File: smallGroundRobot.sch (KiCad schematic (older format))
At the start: 0 parts

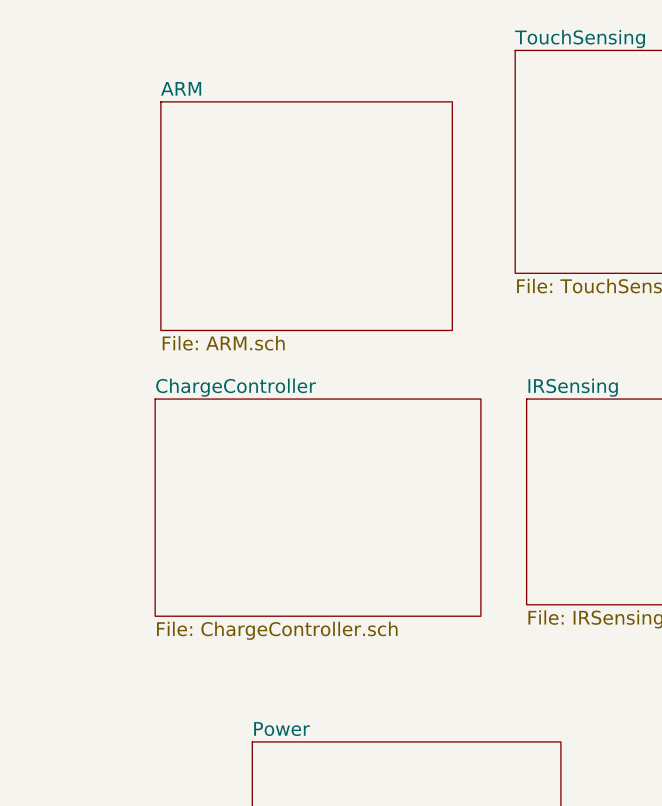
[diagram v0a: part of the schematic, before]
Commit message: Added power, touch, and motor controller
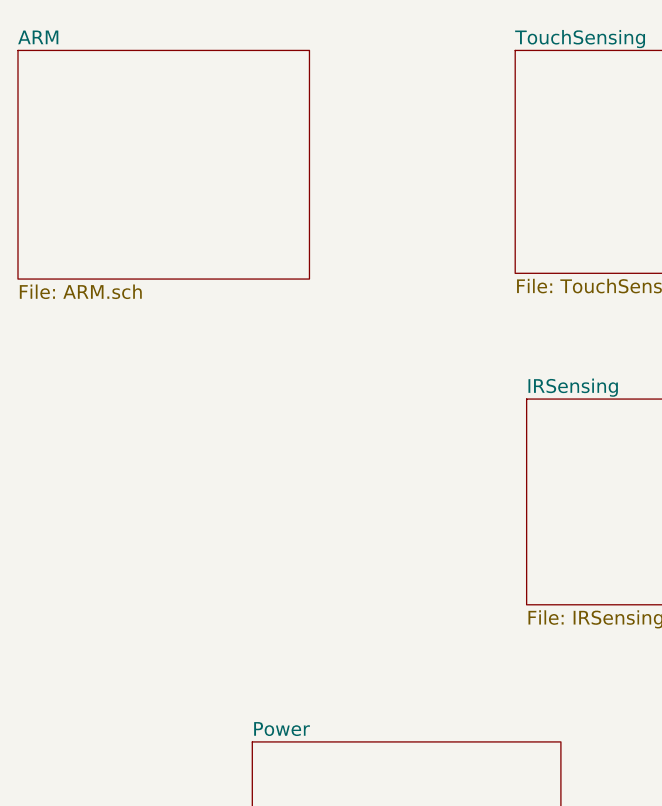
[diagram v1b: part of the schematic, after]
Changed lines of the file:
@@
 $Descr A4 11693 8268
 encoding utf-8
-Sheet 1 8
+Sheet 1 7
 Title ""
 Date ""
@@
 $EndSheet
 $Sheet
-S 4450 2475 1275 1000
+S 3825 2250 1275 1000
 U 5A7E3CFD
 F0 "ARM" 60
@@
 $EndSheet
 $Sheet
-S 4425 3775 1425 950
-U 5A7E3D38
-F0 "ChargeController" 60
-F1 "ChargeController.sch" 60
-$EndSheet
-$Sheet

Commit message: Finished Schematic
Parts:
- added D? (x3): LED, symbol LED
- added J? (x4): Conn_01x03, symbol Conn_01x03
- added J?: USB_OTG, symbol USB_OTG
- added Q? (x2): Q_NPN_BEC, symbol Q_NPN_BEC
- added R? (x2): 2, symbol R
- added R?: 39, symbol R
- added R? (x2): 22, symbol R
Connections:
- new net: J?.2 (Pin_2), Q?.1 (B) (x2)
- new net: Q?.3 (C), R?.2 (x2)
- new net: D?.1 (K), R?.1 (x2)
- new net: J?.2 (D-), R?.2
- new net: J?.3 (D+), R?.2
- new net: D?.1 (K), R?.2
- new net +3V3: J?.1 (Pin_1), J?.1 (Pin_1)
- new net 3V_L1: D?.2 (A), D?.2 (A), J?.3 (Pin_3), J?.3 (Pin_3)
- new net ARM/PB12: D?.2 (A)
- new net D+: R?.1
- new net D-: R?.1
- new net GND: J?.3 (Pin_3), J?.3 (Pin_3), J?.4 (ID), J?.5 (GND), J?.6 (Shield), R?.1
- new net GND_L1: J?.1 (Pin_1), J?.1 (Pin_1), Q?.2 (E), Q?.2 (E)
- new net L1: J?.2 (Pin_2)
- new net L2: J?.2 (Pin_2)
- new net USB5V: J?.1 (VBUS)
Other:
- note added: "Headlights"

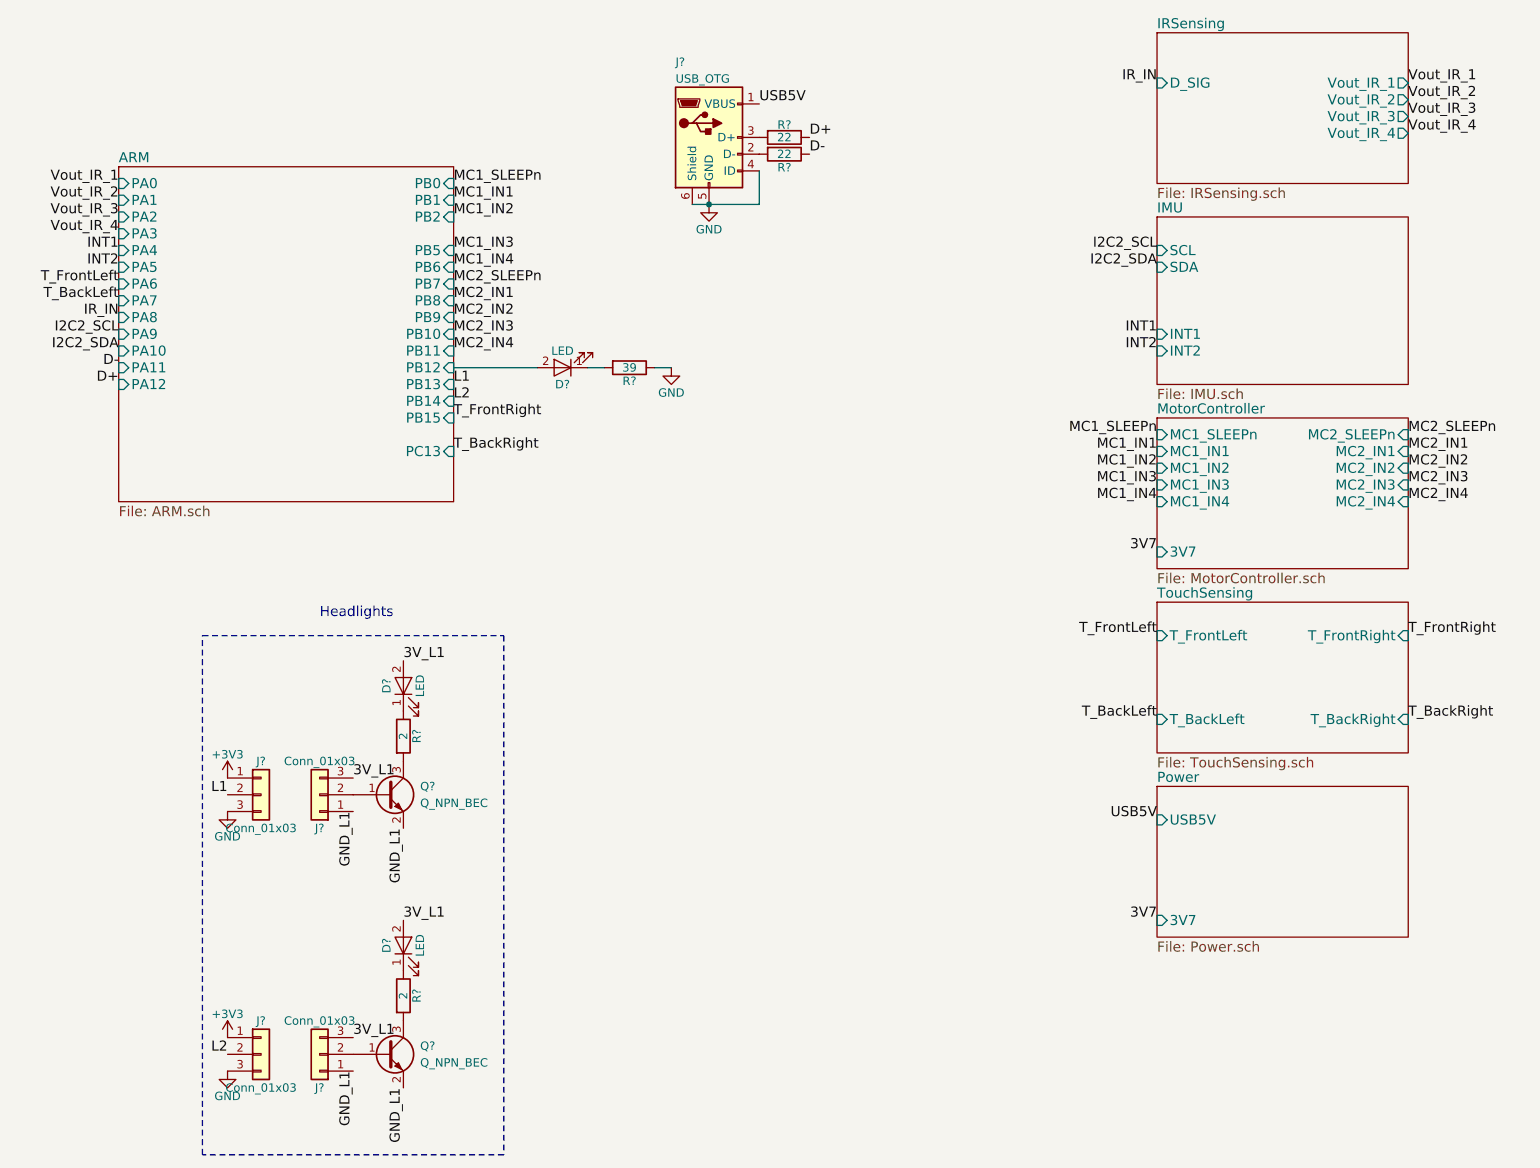
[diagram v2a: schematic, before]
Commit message: Started associating footprints
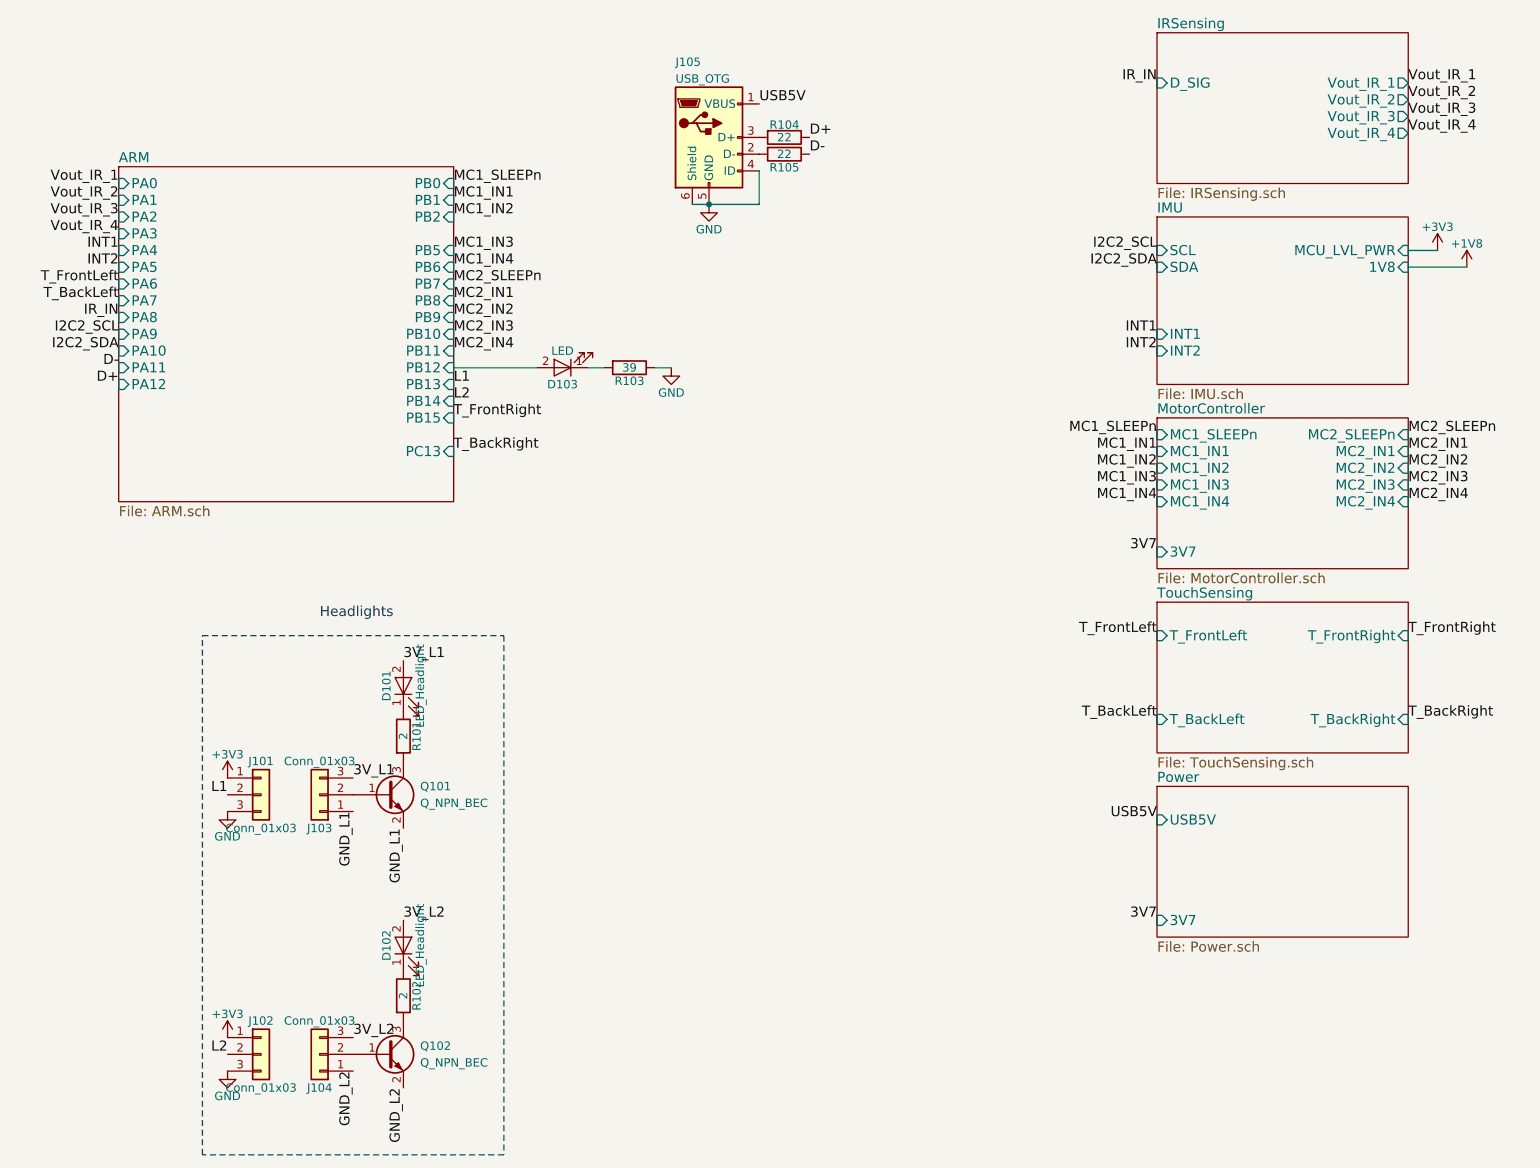
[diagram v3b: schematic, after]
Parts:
- D101, D102: renamed from D?; value LED -> LED_Headlight; footprint (none) -> LEDs:LED_1206
- D103: renamed from D?; footprint (none) -> LEDs:LED_0805
- J101, J102, J103, J104: renamed from J?; footprint (none) -> Pin_Headers:Pin_Header_Angled_1x03_Pitch1.27mm
- J105: renamed from J?; footprint (none) -> Connectors:USB_Micro-B
- gave numbers to parts that had none: 7
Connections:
- net 3V_L1: no longer D102.2 (A), J104.3 (Pin_3)
- net GND_L1: no longer J104.1 (Pin_1), Q102.2 (E)
- new net 3V_L2: D102.2 (A), J104.3 (Pin_3)
- new net GND_L2: J104.1 (Pin_1), Q102.2 (E)
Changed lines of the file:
@@
 F4 "INT1" I L 8000 2500 60
 F5 "INT2" I L 8000 2600 60
+F6 "MCU_LVL_PWR" I R 9500 2000 60
+F7 "1V8" I R 9500 2100 60
 $EndSheet
 $Sheet
@@
 MC2_IN4
 $Comp
-L LED D?
+L LED D103
 U 1 1 5AC53F8E
 P 4450 2700
-F 0 "D?" H 4450 2800 50  0000 C CNN
+F 0 "D103" H 4450 2800 50  0000 C CNN
 F 1 "LED" H 4450 2600 50  0000 C CNN
-F 2 "" H 4450 2700 50  0001 C CNN
+F 2 "LEDs:LED_0805" H 4450 2700 50  0001 C CNN
 F 3 "" H 4450 2700 50  0001 C CNN
 	1    4450 2700
@@
 $EndComp
 $Comp
-L R R?
+L R R103
 U 1 1 5AC54125
 P 4850 2700
-F 0 "R?" V 4930 2700 50  0000 C CNN
+F 0 "R103" V 4930 2700 50  0000 C CNN
 F 1 "39" V 4850 2700 50  0000 C CNN
 F 2 "" V 4780 2700 50  0001 C CNN
@@
 $EndComp
 $Comp
-L GND #PWR?
+L GND #PWR01
 U 1 1 5AC56677
 P 5100 2700
-F 0 "#PWR?" H 5100 2450 50  0001 C CNN
+F 0 "#PWR01" H 5100 2450 50  0001 C CNN
 F 1 "GND" H 5100 2550 50  0000 C CNN
 F 2 "" H 5100 2700 50  0001 C CNN
@@
 	4300 2700 3800 2700
 $Comp
-L Q_NPN_BEC Q?
+L Q_NPN_BEC Q101
 U 1 1 5AC13475
 P 3400 5250
-F 0 "Q?" H 3600 5300 50  0000 L CNN
+F 0 "Q101" H 3600 5300 50  0000 L CNN
 F 1 "Q_NPN_BEC" H 3600 5200 50  0000 L CNN
 F 2 "" H 3600 5350 50  0001 C CNN
@@
 $EndComp
 $Comp
-L R R?
+L R R101
 U 1 1 5AC138C0
 P 3500 4900
-F 0 "R?" V 3580 4900 50  0000 C CNN
+F 0 "R101" V 3580 4900 50  0000 C CNN
 F 1 "2" V 3500 4900 50  0000 C CNN
 F 2 "" V 3430 4900 50  0001 C CNN
@@
 $EndComp
 $Comp
-L LED D?
+L LED D101
 U 1 1 5AC13D61
 P 3500 4600
-F 0 "D?" H 3500 4700 50  0000 C CNN
-F 1 "LED" H 3500 4500 50  0000 C CNN
-F 2 "" H 3500 4600 50  0001 C CNN
+F 0 "D101" H 3500 4700 50  0000 C CNN
+F 1 "LED_Headlight" H 3500 4500 50  0000 C CNN
+F 2 "LEDs:LED_1206" H 3500 4600 50  0001 C CNN
 F 3 "" H 3500 4600 50  0001 C CNN
 	1    3500 4600
@@
 $EndComp
 $Comp
-L Conn_01x03 J?
+L Conn_01x03 J101
 U 1 1 5AC1C60C
 P 2650 5250
-F 0 "J?" H 2650 5450 50  0000 C CNN
+F 0 "J101" H 2650 5450 50  0000 C CNN
 F 1 "Conn_01x03" H 2650 5050 50  0000 C CNN
-F 2 "" H 2650 5250 50  0001 C CNN
+F 2 "Pin_Headers:Pin_Header_Angled_1x03_Pitch1.27mm" H 2650 5250 50  0001 C CNN
 F 3 "" H 2650 5250 50  0001 C CNN
 	1    2650 5250
@@
 $EndComp
 $Comp
-L Conn_01x03 J?
+L Conn_01x03 J103
 U 1 1 5AC1C832
 P 3000 5250
-F 0 "J?" H 3000 5450 50  0000 C CNN
+F 0 "J103" H 3000 5450 50  0000 C CNN
 F 1 "Conn_01x03" H 3000 5050 50  0000 C CNN
-F 2 "" H 3000 5250 50  0001 C CNN
+F 2 "Pin_Headers:Pin_Header_Angled_1x03_Pitch1.27mm" H 3000 5250 50  0001 C CNN
 F 3 "" H 3000 5250 50  0001 C CNN
 	1    3000 5250
 	-1   0    0    1
 $EndComp
-Text Label 3500 4450 0    60   ~ 0
-3V_L1
 Text Label 3200 5150 0    60   ~ 0
 3V_L1
@@
 GND_L1
 $Comp
-L GND #PWR?
+L GND #PWR02
 U 1 1 5AC21B38
 P 2450 5350
-F 0 "#PWR?" H 2450 5100 50  0001 C CNN
+F 0 "#PWR02" H 2450 5100 50  0001 C CNN
 F 1 "GND" H 2450 5200 50  0000 C CNN
 F 2 "" H 2450 5350 50  0001 C CNN
@@
 L1
 $Comp
-L Q_NPN_BEC Q?
+L Q_NPN_BEC Q102
 U 1 1 5AC28944
 P 3400 6800
-F 0 "Q?" H 3600 6850 50  0000 L CNN
+F 0 "Q102" H 3600 6850 50  0000 L CNN
 F 1 "Q_NPN_BEC" H 3600 6750 50  0000 L CNN
 F 2 "" H 3600 6900 50  0001 C CNN
@@
 $EndComp
 $Comp
-L R R?
+L R R102
 U 1 1 5AC2894A
 P 3500 6450
-F 0 "R?" V 3580 6450 50  0000 C CNN
+F 0 "R102" V 3580 6450 50  0000 C CNN
 F 1 "2" V 3500 6450 50  0000 C CNN
 F 2 "" V 3430 6450 50  0001 C CNN
@@
 $EndComp
 $Comp
-L LED D?
+L LED D102
 U 1 1 5AC28950
 P 3500 6150
-F 0 "D?" H 3500 6250 50  0000 C CNN
-F 1 "LED" H 3500 6050 50  0000 C CNN
-F 2 "" H 3500 6150 50  0001 C CNN
+F 0 "D102" H 3500 6250 50  0000 C CNN
+F 1 "LED_Headlight" H 3500 6050 50  0000 C CNN
+F 2 "LEDs:LED_1206" H 3500 6150 50  0001 C CNN
 F 3 "" H 3500 6150 50  0001 C CNN
 	1    3500 6150
@@
 $EndComp
 $Comp
-L Conn_01x03 J?
+L Conn_01x03 J102
 U 1 1 5AC28956
 P 2650 6800
-F 0 "J?" H 2650 7000 50  0000 C CNN
+F 0 "J102" H 2650 7000 50  0000 C CNN
 F 1 "Conn_01x03" H 2650 6600 50  0000 C CNN
-F 2 "" H 2650 6800 50  0001 C CNN
+F 2 "Pin_Headers:Pin_Header_Angled_1x03_Pitch1.27mm" H 2650 6800 50  0001 C CNN
 F 3 "" H 2650 6800 50  0001 C CNN
 	1    2650 6800
@@
 $EndComp
 $Comp
-L Conn_01x03 J?
+L Conn_01x03 J104
 U 1 1 5AC2895C
 P 3000 6800
-F 0 "J?" H 3000 7000 50  0000 C CNN
+F 0 "J104" H 3000 7000 50  0000 C CNN
 F 1 "Conn_01x03" H 3000 6600 50  0000 C CNN
-F 2 "" H 3000 6800 50  0001 C CNN
+F 2 "Pin_Headers:Pin_Header_Angled_1x03_Pitch1.27mm" H 3000 6800 50  0001 C CNN
 F 3 "" H 3000 6800 50  0001 C CNN
 	1    3000 6800
 	-1   0    0    1
 $EndComp
-Text Label 3500 6000 0    60   ~ 0
-3V_L1
 Text Label 3200 6700 0    60   ~ 0
-3V_L1
+3V_L2
 Text Label 3200 6900 3    60   ~ 0
-GND_L1
+GND_L2
 Text Label 3500 7000 3    60   ~ 0
-GND_L1
-$Comp
-L GND #PWR?
+GND_L2
+$Comp
+L GND #PWR03
 U 1 1 5AC2896C
 P 2450 6900
-F 0 "#PWR?" H 2450 6650 50  0001 C CNN
+F 0 "#PWR03" H 2450 6650 50  0001 C CNN
 F 1 "GND" H 2450 6750 50  0000 C CNN
 F 2 "" H 2450 6900 50  0001 C CNN
@@
 Headlights
 $Comp
-L USB_OTG J?
+L USB_OTG J105
 U 1 1 5AC50028
 P 5325 1325
-F 0 "J?" H 5125 1775 50  0000 L CNN
+F 0 "J105" H 5125 1775 50  0000 L CNN
 F 1 "USB_OTG" H 5125 1675 50  0000 L CNN
-F 2 "" H 5475 1275 50  0001 C CNN
+F 2 "Connectors:USB_Micro-B" H 5475 1275 50  0001 C CNN
 F 3 "" H 5475 1275 50  0001 C CNN
 	1    5325 1325
@@
 USB5V
 $Comp
-L GND #PWR?
+L GND #PWR04
 U 1 1 5AC59382
 P 5325 1725
-F 0 "#PWR?" H 5325 1475 50  0001 C CNN
+F 0 "#PWR04" H 5325 1475 50  0001 C CNN
 F 1 "GND" H 5325 1575 50  0000 C CNN
 F 2 "" H 5325 1725 50  0001 C CNN
@@
 Connection ~ 5325 1725
 $Comp
-L R R?
+L R R104
 U 1 1 5AC63839
 P 5775 1325
-F 0 "R?" V 5700 1325 50  0000 C CNN
+F 0 "R104" V 5700 1325 50  0000 C CNN
 F 1 "22" V 5775 1325 50  0000 C CNN
 F 2 "" V 5705 1325 50  0001 C CNN
@@
 $EndComp
 $Comp
-L R R?
+L R R105
 U 1 1 5AC639CC
 P 5775 1425
-F 0 "R?" V 5855 1425 50  0000 C CNN
+F 0 "R105" V 5855 1425 50  0000 C CNN
 F 1 "22" V 5775 1425 50  0000 C CNN
 F 2 "" V 5705 1425 50  0001 C CNN
@@
 $EndComp
 $Comp
-L +3V3 #PWR?
+L +3V3 #PWR05
 U 1 1 5AC7D109
 P 2450 5150
-F 0 "#PWR?" H 2450 5000 50  0001 C CNN
+F 0 "#PWR05" H 2450 5000 50  0001 C CNN
 F 1 "+3V3" H 2450 5290 50  0000 C CNN
 F 2 "" H 2450 5150 50  0001 C CNN
@@
 $EndComp
 $Comp
-L +3V3 #PWR?
+L +3V3 #PWR06
 U 1 1 5AC7D286
 P 2450 6700
-F 0 "#PWR?" H 2450 6550 50  0001 C CNN
+F 0 "#PWR06" H 2450 6550 50  0001 C CNN
 F 1 "+3V3" H 2450 6840 50  0000 C CNN
 F 2 "" H 2450 6700 50  0001 C CNN
@@
 Text Label 1800 2400 2    60   ~ 0
 IR_IN
+$Comp
+L +3V3 #PWR07
+U 1 1 5ACAB9F4
+P 9675 2000
+F 0 "#PWR07" H 9675 1850 50  0001 C CNN
+F 1 "+3V3" H 9675 2140 50  0000 C CNN
+F 2 "" H 9675 2000 50  0001 C CNN
+F 3 "" H 9675 2000 50  0001 C CNN
+	1    9675 2000
+	1    0    0    -1
+$EndComp
+Wire Wire Line
+	9500 2000 9675 2000
+$Comp
+L +1V8 #PWR08
+U 1 1 5ACABC39
+P 9850 2100
+F 0 "#PWR08" H 9850 1950 50  0001 C CNN
+F 1 "+1V8" H 9850 2240 50  0000 C CNN
+F 2 "" H 9850 2100 50  0001 C CNN
+F 3 "" H 9850 2100 50  0001 C CNN
+	1    9850 2100
+	1    0    0    -1
+$EndComp
+Wire Wire Line
+	9500 2100 9850 2100
+Text Label 3500 4450 0    60   ~ 0
+3V_L1
+Text Label 3500 6000 0    60   ~ 0
+3V_L2
 $EndSCHEMATC
